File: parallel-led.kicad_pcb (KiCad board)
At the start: 2 copper layers, 97 x 98 mm, 11 parts

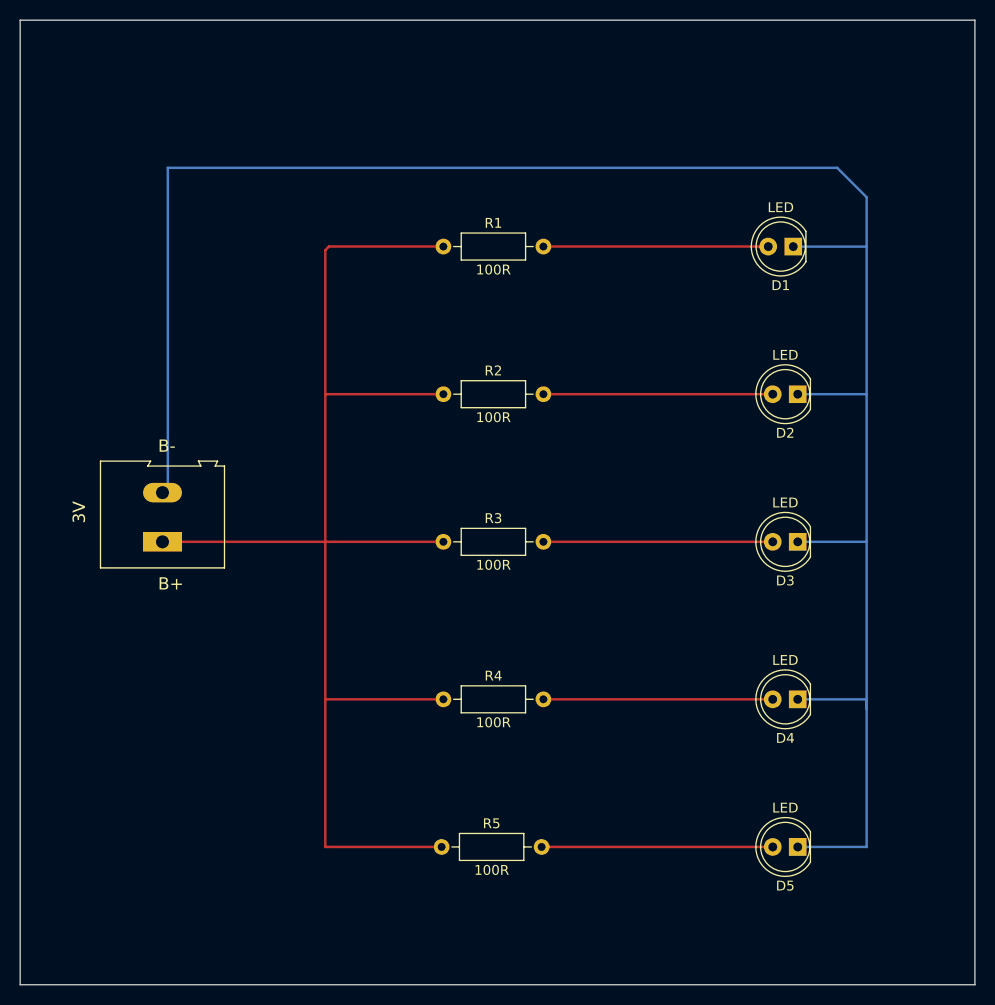
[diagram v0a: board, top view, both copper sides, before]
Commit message: feat: create new footprint to add + and - sign to LED (#1)
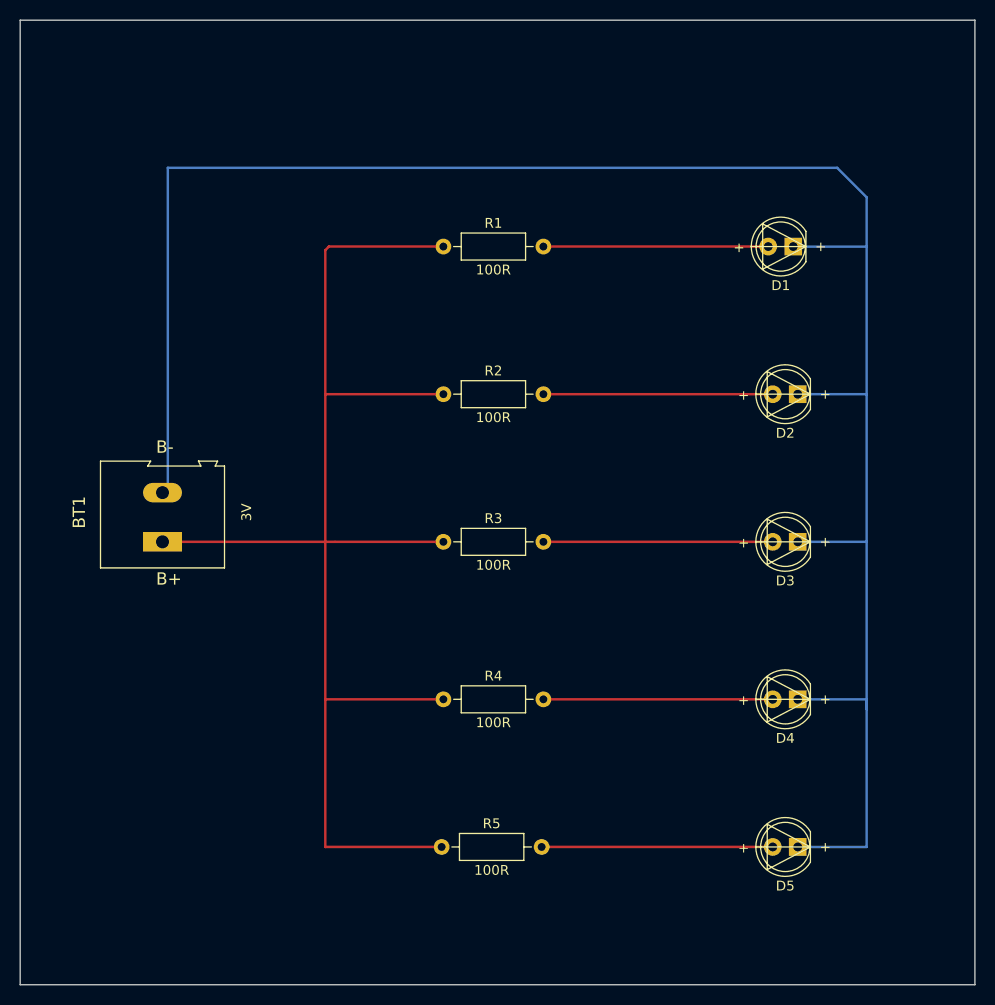
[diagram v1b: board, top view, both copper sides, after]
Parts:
- D1, D2, D3, D4, D5: footprint LED_THT:LED_D5.0mm -> BeginnerModules:BeginnerLED_D5.0mm
- renumbered 3V to BT1
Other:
- board text removed: "B+"
- board text removed: "B-"
